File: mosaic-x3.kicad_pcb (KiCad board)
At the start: 2 copper layers, 21 x 130 mm, 27 parts, among them J1 Conn_01x02, J2 USB_C_Receptacle_USB2.0_14P, J3 LED_STRIP_HEAD, J4 PWR_INJ_1, J5 PWR_INJ_2, J6 PWR_INJ_3, SW1 SW_SPST, SW2 RESET, SW3 BOOT, U1 AMS1117-3.3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

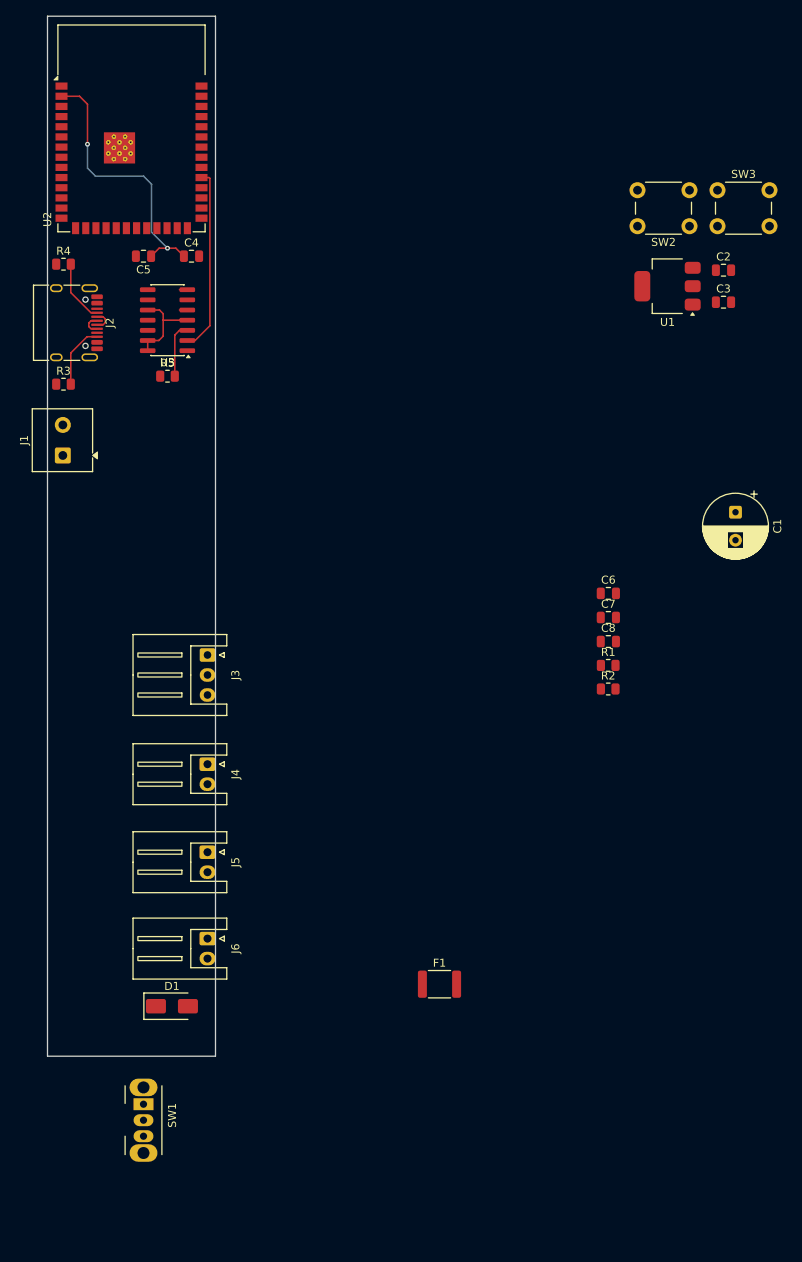
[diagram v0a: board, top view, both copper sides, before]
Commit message: routed pcb and ran drc checks
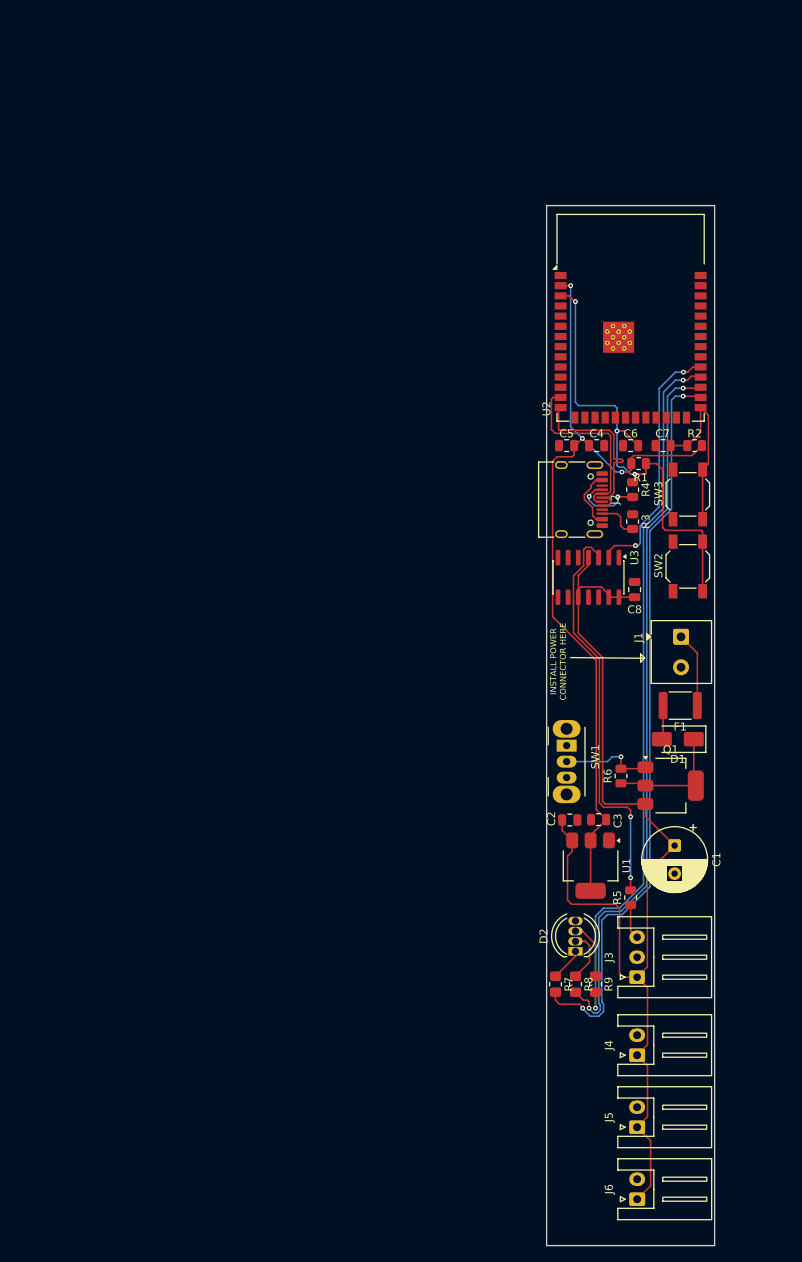
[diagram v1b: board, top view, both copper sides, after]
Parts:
- added D2: LED_RGBK, LED_THT:LED_D5.0mm-4_RGB, F.Cu at (91.0, 141.9)
- added Q1: P-MOSFET, Package_TO_SOT_SMD:SOT-223-3_TabPin2, F.Cu at (102.9, 121.2)
- added R6: 100k, Resistor_SMD:R_0805_2012Metric, F.Cu at (96.7, 120.0)
- added R7: 1k, Resistor_SMD:R_0805_2012Metric_Pad1.20x1.40mm_HandSolder, F.Cu at (88.5, 146.0)
- added R8: 1k, Resistor_SMD:R_0805_2012Metric_Pad1.20x1.40mm_HandSolder, F.Cu at (91.0, 146.0)
- added R9: 1k, Resistor_SMD:R_0805_2012Metric_Pad1.20x1.40mm_HandSolder, F.Cu at (93.5, 146.0)
- SW2, SW3: footprint Button_Switch_THT:SW_PUSH_6mm -> Button_Switch_SMD:SW_SPST_SKQG_WithStem
- moved R5 87.2 mm to (97.9, 135.2), turned to 90 degrees
- moved J1 80.5 mm to (104.2, 102.6), turned to -90 degrees
- moved R4 76.5 mm to (98.1, 84.2), turned to -90 degrees
- moved R3 73.2 mm to (98.1, 88.2), turned to -90 degrees
- moved U1 73.1 mm to (92.9, 131.2), turned to -90 degrees
- moved D1 71.5 mm to (103.8, 115.4), turned to 180 degrees
- moved C2 71.4 mm to (90.3, 125.5)
- moved SW1 69.3 mm to (89.9, 116.2)
- moved J3 67.1 mm to (98.7, 145.1), turned to 90 degrees
- moved J2 66.9 mm to (90.3, 85.4)
- moved U2 66.7 mm to (97.9, 62.7)
- moved C3 66.5 mm to (93.9, 125.4), turned to 180 degrees
- moved J4 64.9 mm to (98.7, 154.9), turned to 90 degrees
- moved J5 63.8 mm to (98.7, 163.9), turned to 90 degrees
- moved J6 62.8 mm to (98.7, 172.9), turned to 90 degrees
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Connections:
- C2 pad 2: Net-(C2-Pad2) -> GND
- C3 pad 2: Net-(C2-Pad2) -> GND
- D1 pad 1: +5V -> Net-(D1-K)
- F1 pad 1: Net-(J1-Pin_2) -> Net-(J1-Pin_1)
- F1 pad 2: Net-(SW1-A) -> Net-(D1-A)
- J1 pad 1: GND -> Net-(J1-Pin_1)
- J1 pad 2: Net-(J1-Pin_2) -> GND
- J2 pad A4: unconnected-(J2-VBUS-PadA4) -> USB_VBUS
- J2 pad A9: unconnected-(J2-VBUS-PadA4)_1 -> USB_VBUS
- J2 pad B4: unconnected-(J2-VBUS-PadA4)_2 -> USB_VBUS
- J2 pad B9: unconnected-(J2-VBUS-PadA4)_3 -> USB_VBUS
- SW1 pad 1: Net-(SW1-A) -> GND
- SW1 pad 2: Net-(D1-A) -> Net-(Q1-G)
- U2 pad 28: unconnected-(U2-IO35-Pad28) -> STATUS_R
- U2 pad 29: unconnected-(U2-IO36-Pad29) -> STATUS_G
- U2 pad 30: unconnected-(U2-IO37-Pad30) -> STATUS_B
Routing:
- net +5V: track 12.4 -> 131.3 mm
- net STATUS_R: track 0.00 -> 93.2 mm, vias 0 -> 2
- net STATUS_G: track 0.00 -> 91.1 mm, vias 0 -> 2
- net STATUS_B: track 0.00 -> 89.0 mm, vias 0 -> 2
- net +3V3: track 34.2 -> 104.1 mm, vias 2 -> 3
- net EN: track 0.00 -> 58.5 mm, vias 0 -> 3
- net Net-(R5-Pad2): track 6.95 -> 50.5 mm, vias 0 -> 2
- net IO0: track 0.00 -> 22.2 mm
- net USB_DP: track 2.74 -> 23.6 mm
- net USB_DM: track 2.74 -> 23.6 mm
- net Net-(D1-K): track 0.00 -> 15.4 mm
- net Net-(Q1-G): track 0.00 -> 11.7 mm, vias 0 -> 1
- net Net-(J1-Pin_1): track 0.00 -> 9.44 mm
- net LED_DATA_3V3: track 23.1 -> 31.8 mm, vias 0 -> 2
- net USB_VBUS: track 0.00 -> 7.62 mm
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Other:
- board text added: "INSTALL POWER CONNECTOR HERE"

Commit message: finished w the pcb board
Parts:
- moved D2 1.40 mm to (92.4, 141.9)
- moved R1 0.81 mm to (99.7, 81.0)
- moved R7 0.50 mm to (89.0, 146.0)
- moved R8 0.50 mm to (91.5, 146.0)
- moved R9 0.50 mm to (94.0, 146.0)
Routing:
- net GND: track 0.00 -> 19.0 mm, vias 0 -> 1
- net EN: track 58.5 -> 53.5 mm
- net STATUS_B: track 89.0 -> 86.8 mm
- net STATUS_R: track 93.2 -> 91.3 mm
- net STATUS_G: track 91.1 -> 89.3 mm
- net +3V3: track 104.1 -> 106.0 mm
- net Net-(D2-RA): track 4.13 -> 5.32 mm
- net +5V: track 131.3 -> 130.5 mm
- net Net-(D2-GA): track 6.54 -> 7.23 mm
- net Net-(R5-Pad2): track 50.5 -> 50.2 mm, vias 2 -> 0
- added copper zone on B.Cu, net GND
- added copper zone on F.Cu, net GND
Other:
- board text added: "ESP32-S3-WROOM-1"
- board text added: "MOSAIC-X3 PCB"
- board text added: "https://shashwat.cc"
- board text added: "made by - @shashwat"
